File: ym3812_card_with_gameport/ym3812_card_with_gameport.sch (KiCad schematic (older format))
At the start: 79 parts, among them IC1 74LS138, IC11 NE558, IC12 74HCT02, IC13 74LS74, IC18 74LS244, IC2 74LS138, IC3 74LS138, IC4 74LS245, IC6 YM3812, IC7 Y3014B, IC8 LM324, IC9 TDA7233, J1 Bus_ISA_8bit, J2 Conn_02x04_Odd_Even, J3 Conn_02x03_Counter_Clockwise

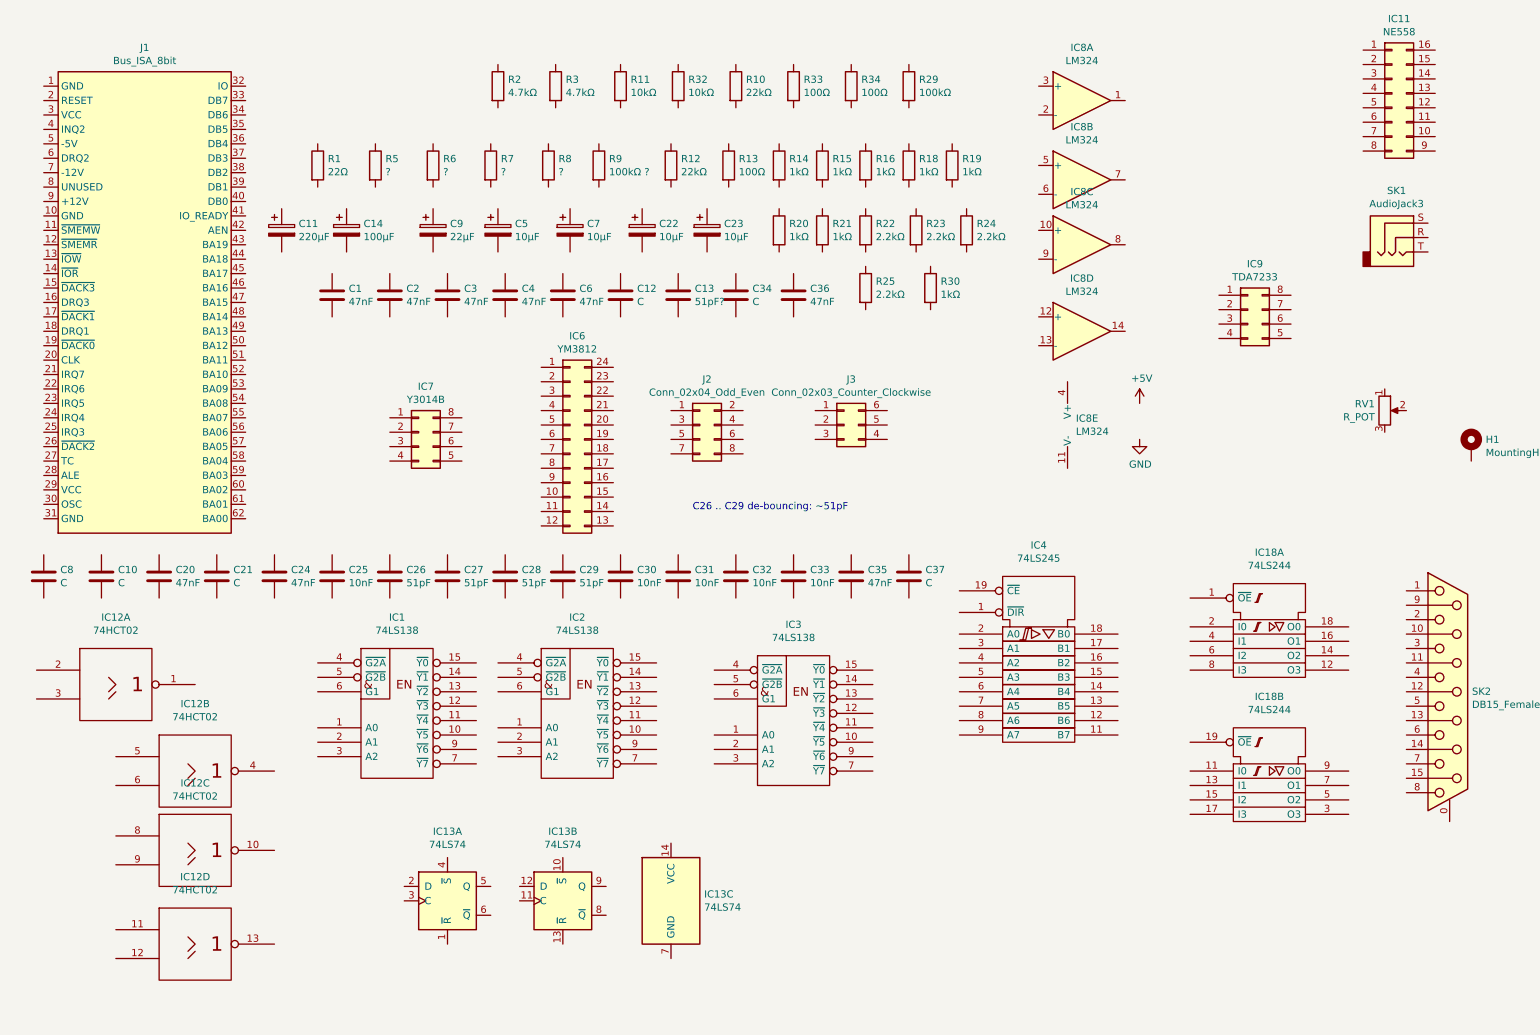
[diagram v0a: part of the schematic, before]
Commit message: some corrections, GND and VCC
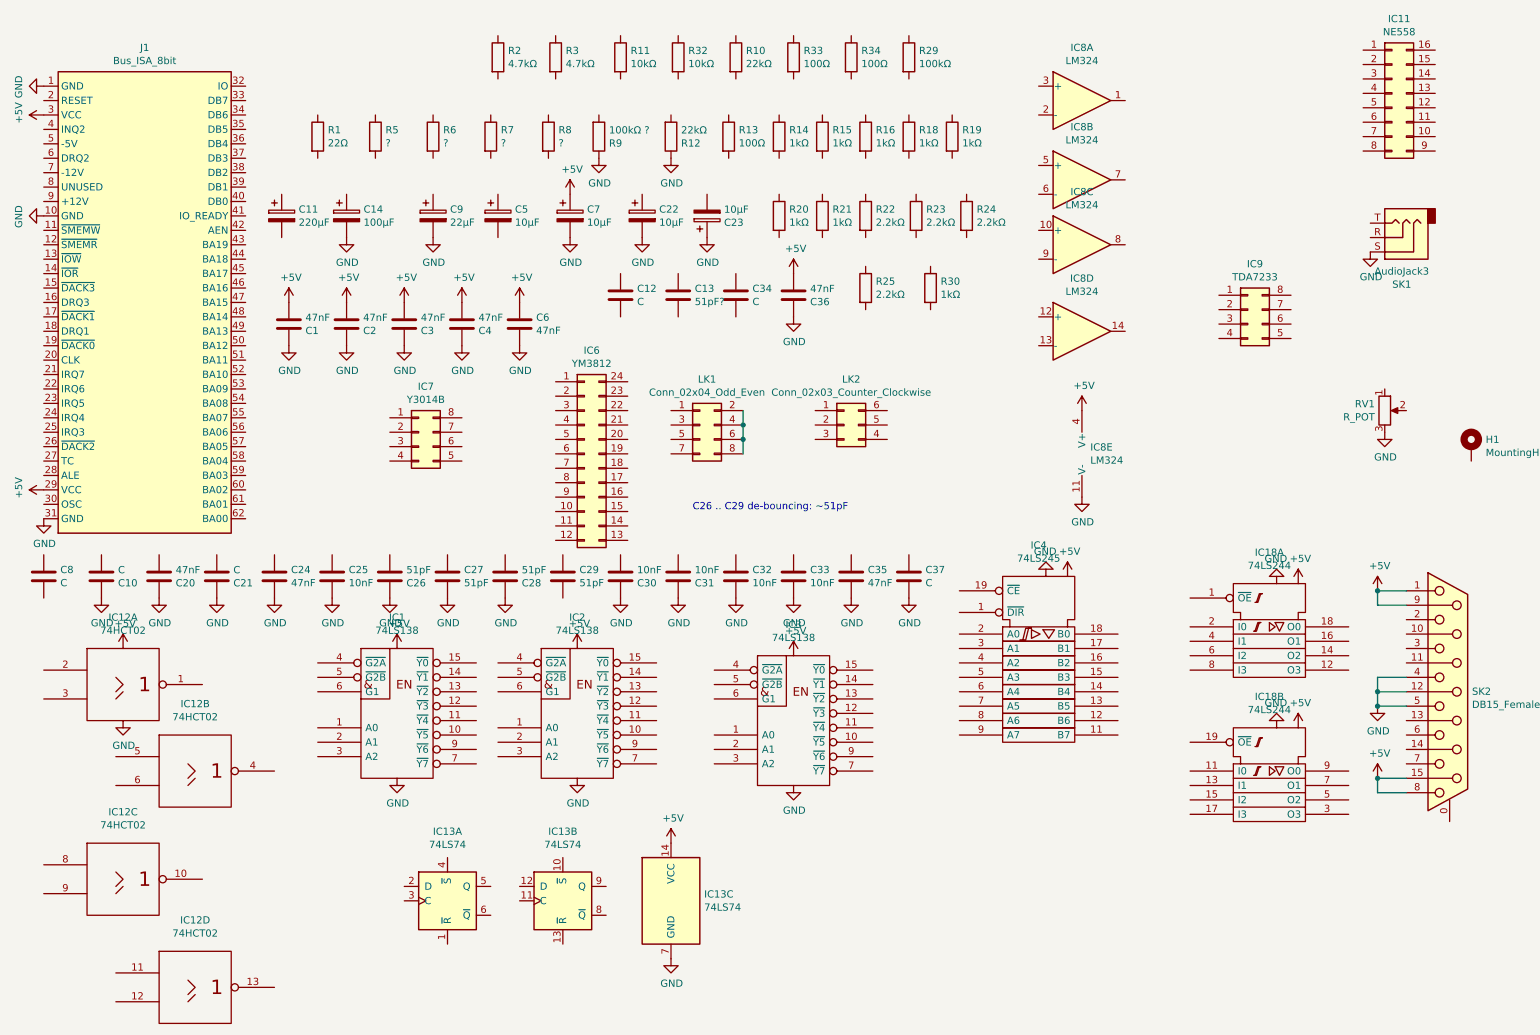
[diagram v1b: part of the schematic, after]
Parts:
- IC1, IC2, IC3: footprint Package_SO:SOIC-14_3.9x8.7mm_P1.27mm -> Package_SO:SOIC-16_3.9x9.9mm_P1.27mm
- renumbered J2 to LK1, J3 to LK2
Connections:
- net VCC is gone; now on net +5V: IC1.16 (VCC), IC12.14 (VCC), IC12.14 (VCC), IC12.14 (VCC), IC12.14 (VCC), IC18.20 (VCC), IC18.20 (VCC), IC2.16 (VCC), IC3.16 (VCC), IC4.20 (VCC)
- net +5V: now also C1.2, C2.2, C3.2, C36.2, C4.2, C6.1, C7.1, IC13.14 (VCC), IC8.4 (V+), J1.29 (VCC), J1.3 (VCC), SK2.1, SK2.15 (P15), SK2.8, SK2.9 (P9)
- net GND: now also C1.1, C10.1, C14.2, C2.1, C20.1, C21.1, C22.2, C23.1, C24.2, C25.2, C26.1, C27.2, C28.1, C3.1, C30.1, C31.1, C32.2, C33.2, C35.2, C36.1, C37.2, C4.1, C6.2, C7.2, C9.2, IC13.7 (GND), IC8.11 (V-), J1.1 (GND), J1.10 (GND), J1.31 (GND), R12.1, R9.1, RV1.3, SK1.S, SK2.12 (P12), SK2.4, SK2.5
- net at LK1.2 (Pin_2): now also LK1.4 (Pin_4), LK1.6 (Pin_6), LK1.8 (Pin_8)
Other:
- moved on the sheet: C1, C11, C14, C2, C22, C23, C3, C4, C5, C6, C7, C9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

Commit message: mostly complete schematic
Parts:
- C21, C34, C37: value C -> 47nF
- LK2: value Conn_02x03_Counter_Clockwise -> Conn_02x03_Odd_Even; symbol Connector_Generic:Conn_02x03_Counter_Clockwise -> Connector_Generic:Conn_02x03_Odd_Even
- R1: value 22Ω -> 8.2kΩ
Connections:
- net +5V: now also C13.2, C24.1, C34.2, C37.1, C5.1, IC11.13 (Pin_13), IC11.5 (Pin_5), IC13.1 (~R), IC13.10 (~S), IC13.13 (~R), IC13.4 (~S), IC6.1 (Pin_1), IC7.1 (Pin_1), R1.1, R10.2, R14.1, R15.2, R16.1, R18.1, R19.1, R20.1, R21.1, R30.2, R5.1, R6.2, R7.2, R8.1; no longer IC8.4 (V+)
- net GND: now also C29.2, C34.1, C5.2, IC11.12 (Pin_12), IC2.5 (~G2B), IC6.12 (Pin_12), IC7.6 (Pin_6), IC8.12 (+), IC8.13 (-), IC8.3 (+), IC9.1 (Pin_1), IC9.2 (Pin_2), IC9.4 (Pin_4), R11.2, R32.1; no longer IC8.11 (V-)
- net at C11.1: now also IC9.5 (Pin_5)
- net AUDIO_OUT: now reaches C11.2
- net AUDIO_OUT: now also R13.2, R32.2, R33.1, R34.2
- net at C14.1: now also IC9.7 (Pin_7)
- net at C9.1: now also IC9.6 (Pin_6)
- net +12V: now reaches C22.1
- net +12V: now also C20.2, C35.1, IC8.4 (V+), IC9.3 (Pin_3), J1.9 (+12V)
- net -12V: now reaches C23.2
- net -12V: now also C21.2, IC8.11 (V-), J1.7 (-12V)
- net BA01_NOR_BA02: now reaches IC1.1 (A0)
- net BA01_NOR_BA02: now also IC12.13, IC2.6 (G1)
- net MAYBE_OPL: now reaches IC1.12 (~Y3)
- net MAYBE_OPL: now also IC2.4 (~G2A)
- net MAYBE_JOYSTICK: now reaches IC1.14 (~Y1)
- net MAYBE_JOYSTICK: now also IC3.4 (~G2A)
- net BA03: now reaches IC1.2 (A1)
- net BA03: now also J1.59 (BA03)
- net BA05: now reaches IC1.3 (A2)
- net BA05: now also J1.57 (BA05)
- net BA06: now reaches IC1.4 (~G2A)
- net BA06: now also J1.56 (BA06)
- net AEN: now reaches IC1.5 (~G2B)
- net AEN: now also J1.42 (AEN)
- net BA09: now reaches IC1.6 (G1)
- net BA09: now also J1.53 (BA09)
- net BA04: now reaches IC2.1 (A0)
- net BA04: now also IC12.3, J1.58 (BA04)
- net P31X: now reaches IC2.10 (~Y5)
- net P31X: now also LK1.5 (Pin_5)
- net P28X: now reaches IC2.13 (~Y2)
- net P28X: now also LK1.3 (Pin_3)
- net P21X: now reaches IC2.14 (~Y1)
- net P21X: now also LK1.1 (Pin_1)
- net BA07: now reaches IC2.2 (A1)
- net BA07: now also IC12.2, J1.55 (BA07)
- net BA08: now reaches IC2.3 (A2)
- net BA08: now also IC3.5 (~G2B), J1.54 (BA08)
- net P38X: now reaches IC2.9 (~Y6)
- net P38X: now also LK1.7 (Pin_7)
- net BA04_NOR_BA07: now reaches IC3.1 (A0)
- net BA04_NOR_BA07: now also IC12.1
- net JOY_OE: now reaches IC3.10 (~Y5)
- net JOY_OE: now also IC18.1 (~OE), IC18.19 (~OE)
- net JOY_TR: now reaches IC3.12 (~Y3)
- net JOY_TR: now also IC11.11 (Pin_11), IC11.14 (Pin_14), IC11.3 (Pin_3), IC11.6 (Pin_6)
- net IOR: now reaches IC3.2 (A1)
- net IOR: now also IC4.1 (~DIR), IC6.6 (Pin_6), J1.14 (~IOR)
- net IOW: now reaches IC3.3 (A2)
- net IOW: now also IC6.5 (Pin_5), J1.13 (~IOW)
- net BA00: now reaches IC3.6 (G1)
- net BA00: now also IC6.4 (Pin_4), J1.62 (BA00)
- net OPL_D7: now reaches IC4.11 (B7)
- net OPL_D7: now also IC6.18 (Pin_18)
- net OPL_D6: now reaches IC4.12 (B6)
- net OPL_D6: now also IC6.17 (Pin_17)
- net OPL_D5: now reaches IC4.13 (B5)
- net OPL_D5: now also IC6.16 (Pin_16)
- net OPL_D4: now reaches IC4.14 (B4)
- net OPL_D4: now also IC6.15 (Pin_15)
- net OPL_D3: now reaches IC4.15 (B3)
- net OPL_D3: now also IC6.14 (Pin_14)
- net OPL_D2: now reaches IC4.16 (B2)
- net OPL_D2: now also IC6.13 (Pin_13)
- net OPL_D1: now reaches IC4.17 (B1)
- net OPL_D1: now also IC6.11 (Pin_11)
- net OPL_D0: now reaches IC4.18 (B0)
- net OPL_D0: now also IC6.10 (Pin_10)
- net OPL_CS: now reaches IC4.19 (~CE)
- net OPL_CS: now also IC6.7 (Pin_7), LK1.2 (Pin_2), LK1.4 (Pin_4), LK1.6 (Pin_6), LK1.8 (Pin_8)
- net DB0: now reaches IC4.2 (A0)
- net DB0: now also IC18.18 (O0), J1.40 (DB0)
- net DB1: now reaches IC4.3 (A1)
- net DB1: now also IC18.16 (O1), J1.39 (DB1)
- net DB2: now reaches IC4.4 (A2)
- net DB2: now also IC18.14 (O2), J1.38 (DB2)
- net DB3: now reaches IC4.5 (A3)
- net DB3: now also IC18.12 (O3), J1.37 (DB3)
- net DB4: now reaches IC4.6 (A4)
- net DB4: now also IC18.3 (O3), J1.36 (DB4)
- net DB5: now reaches IC4.7 (A5)
- net DB5: now also IC18.5 (O2), J1.35 (DB5)
- net DB6: now reaches IC4.8 (A6)
- net DB6: now also IC18.7 (O1), J1.34 (DB6)
- net DB7: now reaches IC4.9 (A7)
- net DB7: now also IC18.9 (O0), J1.33 (DB7)
- net IRQ: now reaches IC12.4
- net IRQ: now also LK2.2 (Pin_2), LK2.4 (Pin_4), LK2.6 (Pin_6)
- net OPL_IRQ: now reaches IC12.5
- net OPL_IRQ: now also IC12.6, IC6.2 (Pin_2), R1.2
- net OPL_IC: now reaches IC12.10
- net OPL_IC: now also IC6.3 (Pin_3)
- net RESET: now reaches IC12.8
- net RESET: now also IC12.9, J1.2 (RESET)
- net BA02: now reaches IC12.11
- net BA02: now also J1.60 (BA02)
- net BA01: now reaches IC12.12
- net BA01: now also J1.61 (BA01)
- net QA: now reaches IC18.2 (I0)
- net QA: now also IC11.1 (Pin_1), R18.2
- net QB: now reaches IC18.4 (I1)
- net QB: now also IC11.8 (Pin_8), R19.2
- net QC: now reaches IC18.6 (I2)
- net QC: now also IC11.9 (Pin_9), R20.2
- net QD: now reaches IC18.8 (I3)
- net QD: now also IC11.16 (Pin_16), R21.2
- net BTN4: now reaches IC18.11 (I0)
- net BTN4: now also C28.2, R16.2, SK2.14 (P14)
- net BTN3: now reaches IC18.13 (I1)
- net BTN3: now also C27.1, R15.1, SK2.10 (P10)
- net BTN2: now reaches IC18.15 (I2)
- net BTN2: now also C26.2, R14.2, SK2.7
- net BTN1: now reaches IC18.17 (I3)
- net BTN1: now also C29.1, R30.1, SK2.2
- net PREAMP_OUT: now reaches IC8.1
- net PREAMP_OUT: now also C8.1, R9.2
- net at IC8.2 (-): now also C13.1, R10.1, R29.2
- net at IC8.5 (+): now also R3.2
- net at IC8.6 (-): now also R2.2
- net at IC8.7: now also R2.1, RV1.1
- net DAC_REF: now reaches IC8.10 (+)
- net DAC_REF: now also IC7.7 (Pin_7)
- net DAC_MP: now reaches IC8.8
- net DAC_MP: now also IC7.8 (Pin_8), IC8.9 (-), R11.1
- net at RV1.2: now also C12.1
- net JOY3: now reaches SK2.11 (P111)
- net JOY3: now also R24.2, R6.1
- net JOY4: now reaches SK2.13 (P13)
- net JOY4: now also R25.2, R8.2
- net JOY1: now reaches SK2.3
- net JOY1: now also R22.2, R7.1
- net JOY2: now reaches SK2.6
- net JOY2: now also R23.2, R5.2
- net at SK1.R: now also R34.1
- net at SK1.T: now also R33.2
- net IRQ3: now reaches LK2.1 (Pin_1)
- net IRQ3: now also J1.25 (IRQ3)
- net IRQ5: now reaches LK2.3 (Pin_3)
- net IRQ5: now also J1.23 (IRQ5)
- net IRQ2: now reaches LK2.5 (Pin_5)
- net IRQ2: now also J1.4 (INQ2)
- net OSC: now reaches J1.30 (OSC)
- net OSC: now also IC13.11 (C)
- net DAC_OUT: now reaches R3.1
- net DAC_OUT: now also IC7.2 (Pin_2)
- net at R29.1: now also C12.2
- net VIN: now reaches R12.2
- net VIN: now also C8.2, IC9.8 (Pin_8)
- net at R13.1: now also C10.2
- net OPL_SH: now reaches IC7.3 (Pin_3)
- net OPL_SH: now also IC6.20 (Pin_20)
- net OPL_OUT: now reaches IC7.4 (Pin_4)
- net OPL_OUT: now also IC6.21 (Pin_21)
- net OPL_SY: now reaches IC7.5 (Pin_5)
- net OPL_SY: now also IC6.23 (Pin_23)
- net OPL_CLK: now reaches IC6.24 (Pin_24)
- net OPL_CLK: now also IC13.5 (Q)
- net at IC13.2 (D): now also IC13.6 (~Q)
- net at IC13.3 (C): now also IC13.9 (Q)
- net at IC13.12 (D): now also IC13.8 (~Q)
- net TIMING_C: now reaches IC11.10 (Pin_10)
- net TIMING_C: now also C31.2, R23.1
- net TIMING_D: now reaches IC11.15 (Pin_15)
- net TIMING_D: now also C30.2, R22.1
- net TIMING_A: now reaches IC11.2 (Pin_2)
- net TIMING_A: now also C33.1, R25.1
- net VCTL: now reaches IC11.4 (Pin_4)
- net VCTL: now also C25.1
- net TIMING_B: now reaches IC11.7 (Pin_7)
- net TIMING_B: now also C32.1, R24.1
- no-connect marks 0 -> 52
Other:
- note added: "Address decoding"
- note added: "Power supply and filtering"
- note added: "speculative"
- note removed: "C26 .. C29 de-bouncing: ~~51pF"
- moved on the sheet: C1, C10, C11, C12, C13, C14, C2, C20, C21, C22, C23, C24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
